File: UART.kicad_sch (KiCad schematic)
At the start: 2 parts

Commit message: PCB drawn
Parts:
- C5: value (none) -> 100n; footprint (none) -> Capacitor_SMD:C_0603_1608Metric
- U2: value (none) -> CH340E; footprint (none) -> Package_SO:MSOP-10_3x3mm_P0.5mm
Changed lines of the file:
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@@
       (effects (font (size 1.27 1.27)) (justify right))
     )
-    (property "Value" "" (id 1) (at 117.856 87.63 0)
+    (property "Value" "100n" (id 1) (at 117.856 87.63 0)
       (effects (font (size 1.27 1.27)) (justify right))
     )
-    (property "Footprint" "" (id 2) (at 116.84 85.09 0)
+    (property "Footprint" "Capacitor_SMD:C_0603_1608Metric" (id 2) (at 116.84 85.09 0)
       (effects (font (size 1.27 1.27)) hide)
     )
@@
   (symbol (lib_id "power:GND") (at 116.84 90.17 0) (unit 1)
     (in_bom yes) (on_board yes) (fields_autoplaced)
-    (property "Reference" "#PWR?" (id 0) (at 116.84 96.52 0)
+    (property "Reference" "#PWR0118" (id 0) (at 116.84 96.52 0)
       (effects (font (size 1.27 1.27)) hide)
     )
-    (property "Value" "" (id 1) (at 116.84 94.7325 0))
+    (property "Value" "GND" (id 1) (at 116.84 94.7325 0))
     (property "Footprint" "" (id 2) (at 116.84 90.17 0)
       (effects (font (size 1.27 1.27)) hide)
@@
       (effects (font (size 1.27 1.27)) (justify left))
     )
-    (property "Value" "" (id 1) (at 142.9894 105.2546 0)
+    (property "Value" "CH340E" (id 1) (at 142.9894 105.2546 0)
       (effects (font (size 1.27 1.27)) (justify left))
     )
-    (property "Footprint" "" (id 2) (at 142.24 101.6 0)
+    (property "Footprint" "Package_SO:MSOP-10_3x3mm_P0.5mm" (id 2) (at 142.24 101.6 0)
       (effects (font (size 1.27 1.27)) (justify left) hide)
     )
@@
   (symbol (lib_id "power:GND") (at 140.97 104.14 0) (unit 1)
     (in_bom yes) (on_board yes) (fields_autoplaced)
-    (property "Reference" "#PWR?" (id 0) (at 140.97 110.49 0)
+    (property "Reference" "#PWR0119" (id 0) (at 140.97 110.49 0)
       (effects (font (size 1.27 1.27)) hide)
     )
-    (property "Value" "" (id 1) (at 140.97 108.7025 0))
+    (property "Value" "GND" (id 1) (at 140.97 108.7025 0))
     (property "Footprint" "" (id 2) (at 140.97 104.14 0)
       (effects (font (size 1.27 1.27)) hide)

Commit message: Change the map and rebuild the PCB
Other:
- moved on the sheet: C5
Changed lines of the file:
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@@
     (stroke (width 0) (type default) (color 0 0 0 0))
   )
-  (wire (pts (xy 116.84 87.63) (xy 116.84 90.17))
+  (wire (pts (xy 111.76 87.63) (xy 111.76 90.17))
     (stroke (width 0) (type default) (color 0 0 0 0))
   )
-  (wire (pts (xy 114.3 78.74) (xy 116.84 78.74))
+  (wire (pts (xy 109.22 78.74) (xy 111.76 78.74))
     (stroke (width 0) (type default) (color 0 0 0 0))
   )
@@
     (stroke (width 0) (type default) (color 0 0 0 0))
   )
-  (wire (pts (xy 116.84 78.74) (xy 116.84 82.55))
+  (wire (pts (xy 111.76 78.74) (xy 111.76 82.55))
     (stroke (width 0) (type default) (color 0 0 0 0))
   )
@@
     (effects (font (size 1.27 1.27)) (justify left))
   )
-  (hierarchical_label "3V3" (shape input) (at 114.3 78.74 180)
+  (hierarchical_label "3V3" (shape input) (at 109.22 78.74 180)
     (effects (font (size 1.27 1.27)) (justify right))
   )
@@
     (effects (font (size 1.27 1.27)) (justify left))
   )
-  (symbol (lib_id "Device:C_Small") (at 116.84 85.09 0) (mirror y) (unit 1)
+  (symbol (lib_id "Device:C_Small") (at 111.76 85.09 0) (mirror y) (unit 1)
     (in_bom yes) (on_board yes)
-    (property "Reference" "C5" (id 0) (at 118.11 83.058 0)
+    (property "Reference" "C5" (id 0) (at 113.03 83.058 0)
       (effects (font (size 1.27 1.27)) (justify right))
     )
-    (property "Value" "100n" (id 1) (at 117.856 87.63 0)
+    (property "Value" "100n" (id 1) (at 112.776 87.63 0)
       (effects (font (size 1.27 1.27)) (justify right))
     )
-    (property "Footprint" "Capacitor_SMD:C_0603_1608Metric" (id 2) (at 116.84 85.09 0)
+    (property "Footprint" "Capacitor_SMD:C_0603_1608Metric" (id 2) (at 111.76 85.09 0)
       (effects (font (size 1.27 1.27)) hide)
     )
-    (property "Datasheet" "~" (id 3) (at 116.84 85.09 0)
+    (property "Datasheet" "~" (id 3) (at 111.76 85.09 0)
       (effects (font (size 1.27 1.27)) hide)
     )
@@
     (pin "2")
   )
-  (symbol (lib_id "power:GND") (at 116.84 90.17 0) (unit 1)
+  (symbol (lib_id "power:GND") (at 140.97 104.14 0) (unit 1)
     (in_bom yes) (on_board yes) (fields_autoplaced)
-    (property "Reference" "#PWR0118" (id 0) (at 116.84 96.52 0)
+    (property "Reference" "#PWR0128" (id 0) (at 140.97 110.49 0)
       (effects (font (size 1.27 1.27)) hide)
     )
-    (property "Value" "GND" (id 1) (at 116.84 94.7325 0))
-    (property "Footprint" "" (id 2) (at 116.84 90.17 0)
+    (property "Value" "GND" (id 1) (at 140.97 108.7025 0))
+    (property "Footprint" "" (id 2) (at 140.97 104.14 0)
       (effects (font (size 1.27 1.27)) hide)
     )
-    (property "Datasheet" "" (id 3) (at 116.84 90.17 0)
+    (property "Datasheet" "" (id 3) (at 140.97 104.14 0)
       (effects (font (size 1.27 1.27)) hide)
     )
@@
     (pin "9")
   )
-  (symbol (lib_id "power:GND") (at 140.97 104.14 0) (unit 1)
+  (symbol (lib_id "power:GND") (at 111.76 90.17 0) (unit 1)
     (in_bom yes) (on_board yes) (fields_autoplaced)
-    (property "Reference" "#PWR0119" (id 0) (at 140.97 110.49 0)
+    (property "Reference" "#PWR0127" (id 0) (at 111.76 96.52 0)
       (effects (font (size 1.27 1.27)) hide)
     )
-    (property "Value" "GND" (id 1) (at 140.97 108.7025 0))
-    (property "Footprint" "" (id 2) (at 140.97 104.14 0)
+    (property "Value" "GND" (id 1) (at 111.76 94.7325 0))
+    (property "Footprint" "" (id 2) (at 111.76 90.17 0)
       (effects (font (size 1.27 1.27)) hide)
     )
-    (property "Datasheet" "" (id 3) (at 140.97 104.14 0)
+    (property "Datasheet" "" (id 3) (at 111.76 90.17 0)
       (effects (font (size 1.27 1.27)) hide)
     )

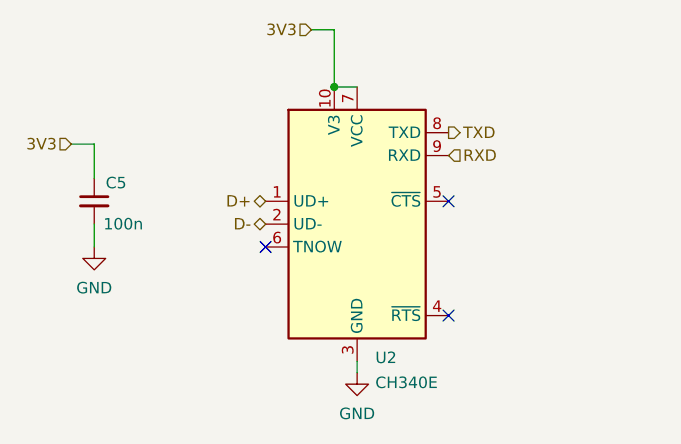
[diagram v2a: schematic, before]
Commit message: Add ESD protection
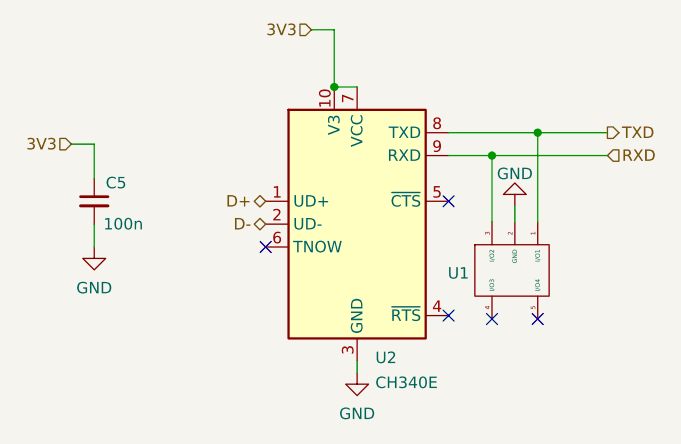
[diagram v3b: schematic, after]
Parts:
- added U1: ~, Package_TO_SOT_SMD:SOT-23-5, symbol Extra IC:ESDS314
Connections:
- net GND: now also U1.2 (GND)
- net RXD: now also U1.3 (I/O2)
- net TXD: now also U1.1 (I/O1)
- no-connect marks 3 -> 5
